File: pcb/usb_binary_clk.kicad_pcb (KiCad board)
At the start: 2 copper layers, 55.6 x 77.4 mm, 42 parts, among them J1 USB_B_Micro, J2 USB_B_Micro, J3 AVR-ISP-6, SW1 SW_Push, SW2 SW_Push, SW3 SW_Push, U1 MCP7940N-xP, U2 ATtiny84V-10PU, Y1 Crystal

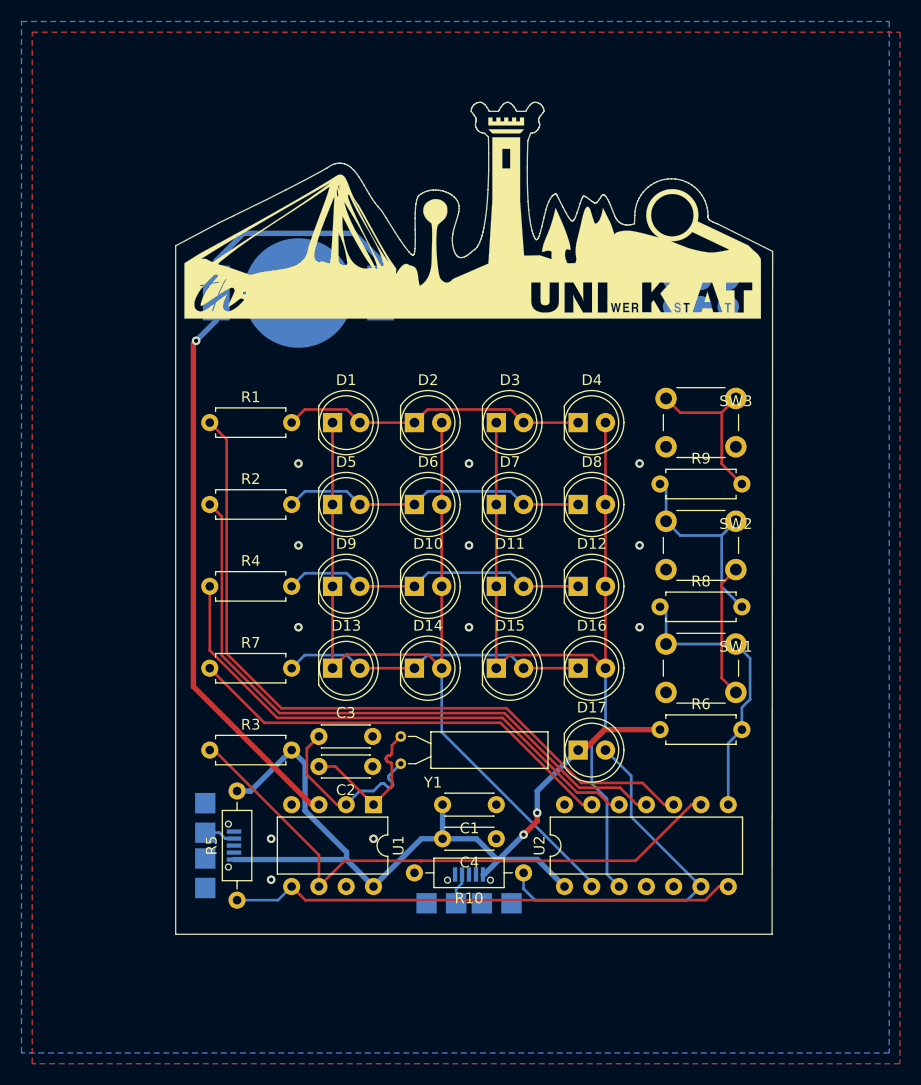
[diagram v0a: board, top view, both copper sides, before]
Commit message: rearrange footprint references + add icons
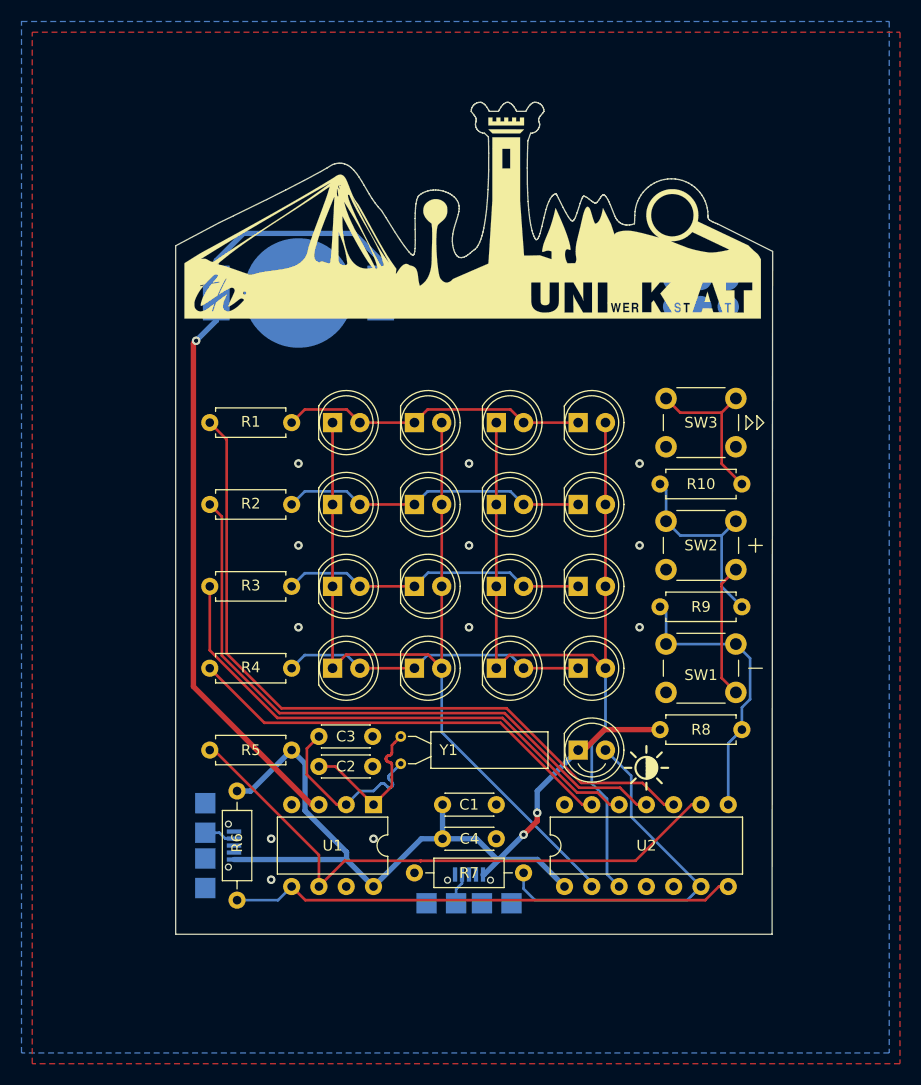
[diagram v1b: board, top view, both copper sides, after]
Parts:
- renumbered R9 to R10, R4 to R3, R7 to R4, R3 to R5, R5 to R6, R10 to R7, R6 to R8, R8 to R9

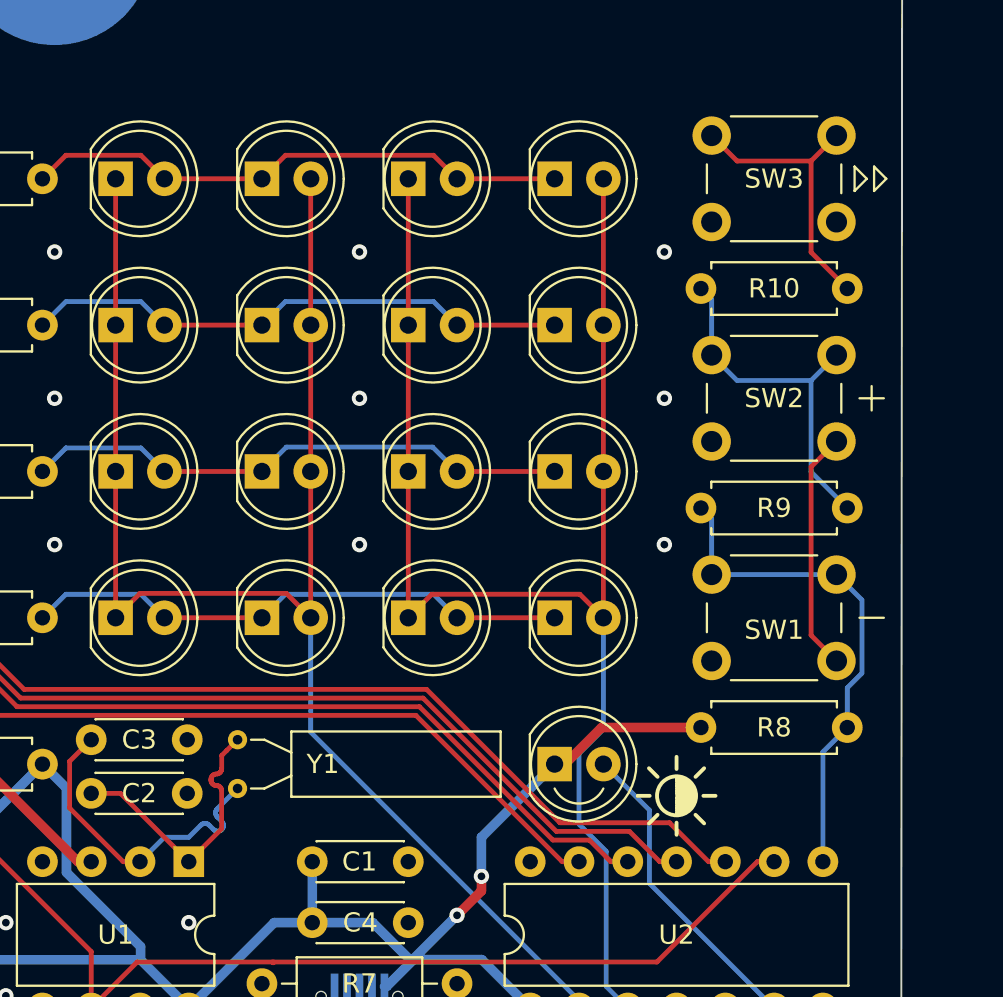
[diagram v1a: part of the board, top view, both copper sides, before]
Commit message: connect programmer; add qr code; create gerber files for first order
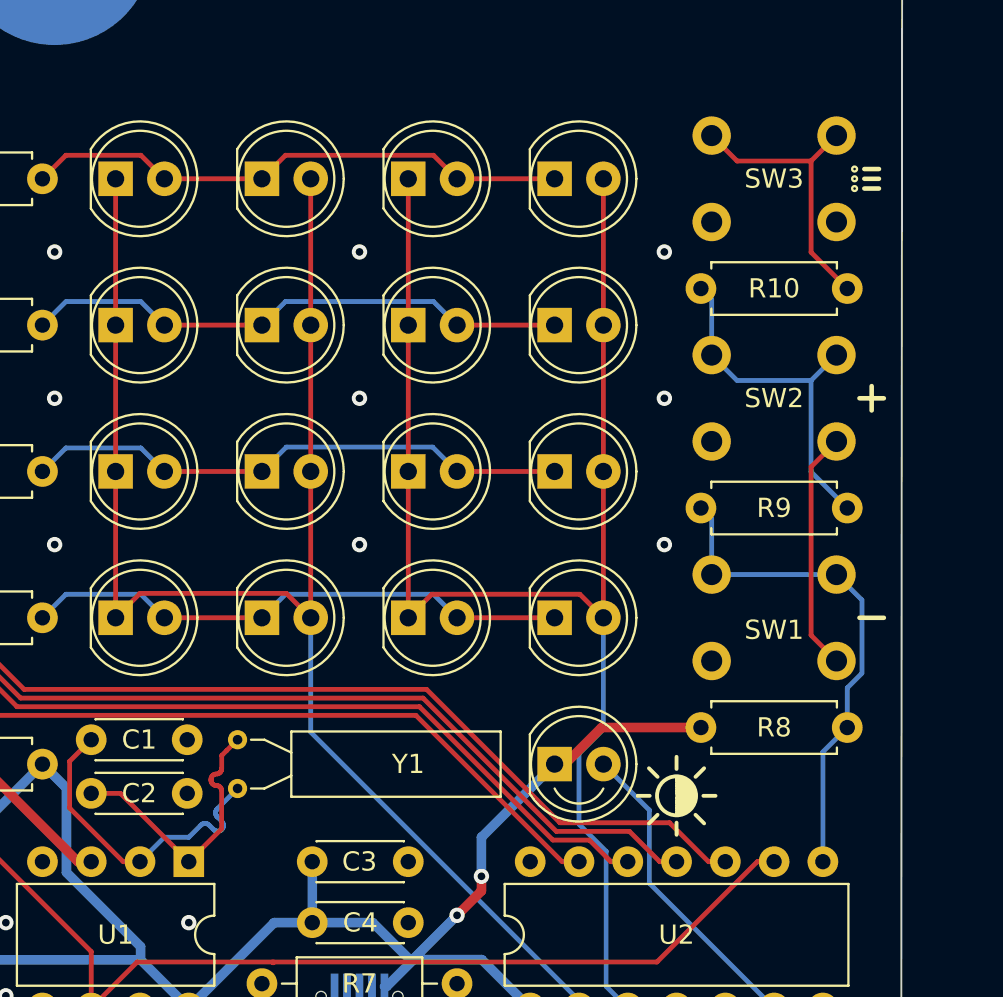
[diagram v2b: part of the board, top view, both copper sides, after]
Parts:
- SW1, SW2, SW3: footprint custom:SW_PUSH_6mm_H4.3mm -> binary_clk_parts:SW_PUSH_6mm_H4.3mm_nosilk
- renumbered C3 to C1, C1 to C3

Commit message: safety commit
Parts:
- added G***: LOGO, binary_clk_parts:qr_code_unikat, B.Cu at (169.5, 46.4)
- moved J3 19.7 mm to (155.6, 46.4), turned to 180 degrees
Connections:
- J3 pad 1: Net-(J3-Pad1) -> /MISO
- J3 pad 2: Net-(J3-Pad2) -> +5V
- J3 pad 3: Net-(J3-Pad3) -> /SCK
- J3 pad 4: Net-(J3-Pad4) -> /MOSI
- J3 pad 5: Net-(J3-Pad5) -> /RST
- J3 pad 6: Net-(J3-Pad6) -> GND
- R5 pad 1: /scl -> /SCK
- R6 pad 1: /sda -> /MOSI
- R8 pad 2: /sw -> /MISO
- R9 pad 1: /sw -> /MISO
- SW1 pad 1: /sw -> /MISO
- U1 pad 5: /sda -> /MOSI
- U1 pad 6: /scl -> /SCK
- U2 pad 4: Net-(U2-Pad4) -> /RST
- U2 pad 7: /sda -> /MOSI
- U2 pad 8: /sw -> /MISO
- U2 pad 9: /scl -> /SCK
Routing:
- net /MOSI: track 0.00 -> 123.9 mm, vias 0 -> 1
- net /SCK: track 0.00 -> 113.7 mm
- net /RST: track 0.00 -> 67.4 mm, vias 0 -> 3
- net /MISO: track 0.00 -> 59.4 mm
- net /scl: track 55.9 -> 0.00 mm
- net /sda: track 47.3 -> 0.00 mm
- net +5V: track 81.4 -> 128.1 mm, vias 2 -> 3
- net /sw: track 26.5 -> 0.00 mm
- net GND: vias 12 -> 13

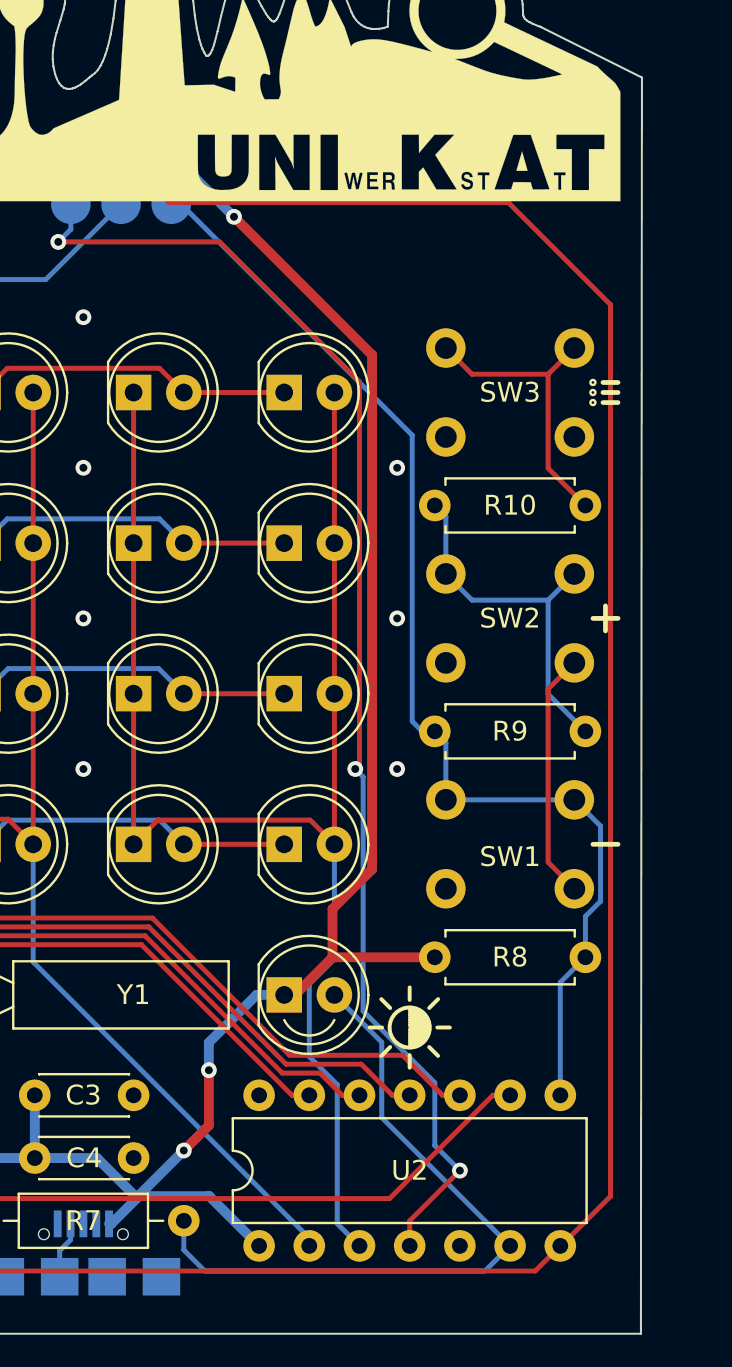
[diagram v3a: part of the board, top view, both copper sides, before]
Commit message: move via out of printed part
fix #4
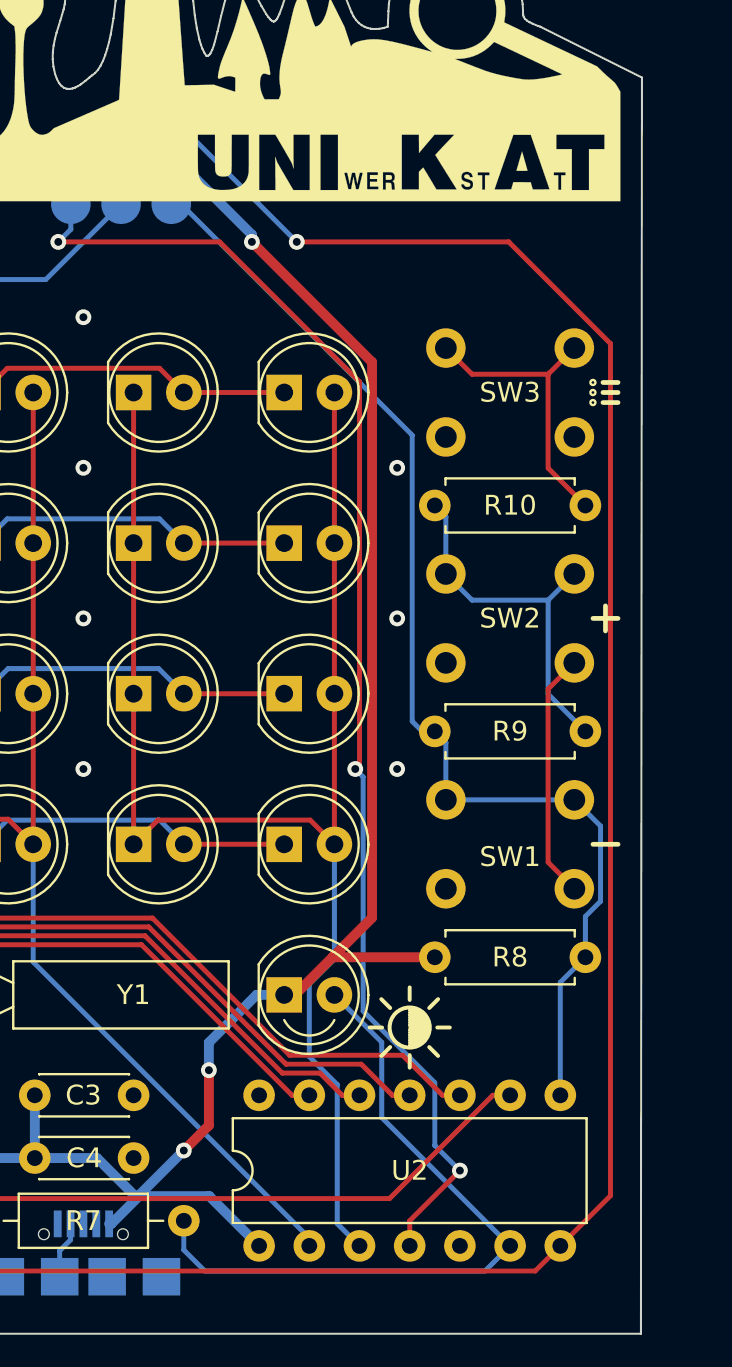
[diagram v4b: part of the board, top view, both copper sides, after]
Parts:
- moved G*** 1.91 mm to (171.4, 46.4)
